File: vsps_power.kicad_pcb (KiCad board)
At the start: 2 copper layers, 84.5 x 85 mm, 11 parts, among them J1 OUT, P1 Conn_WallPlug_Earth, SW1 SW_SPST, T1 Transformer_2P_2S

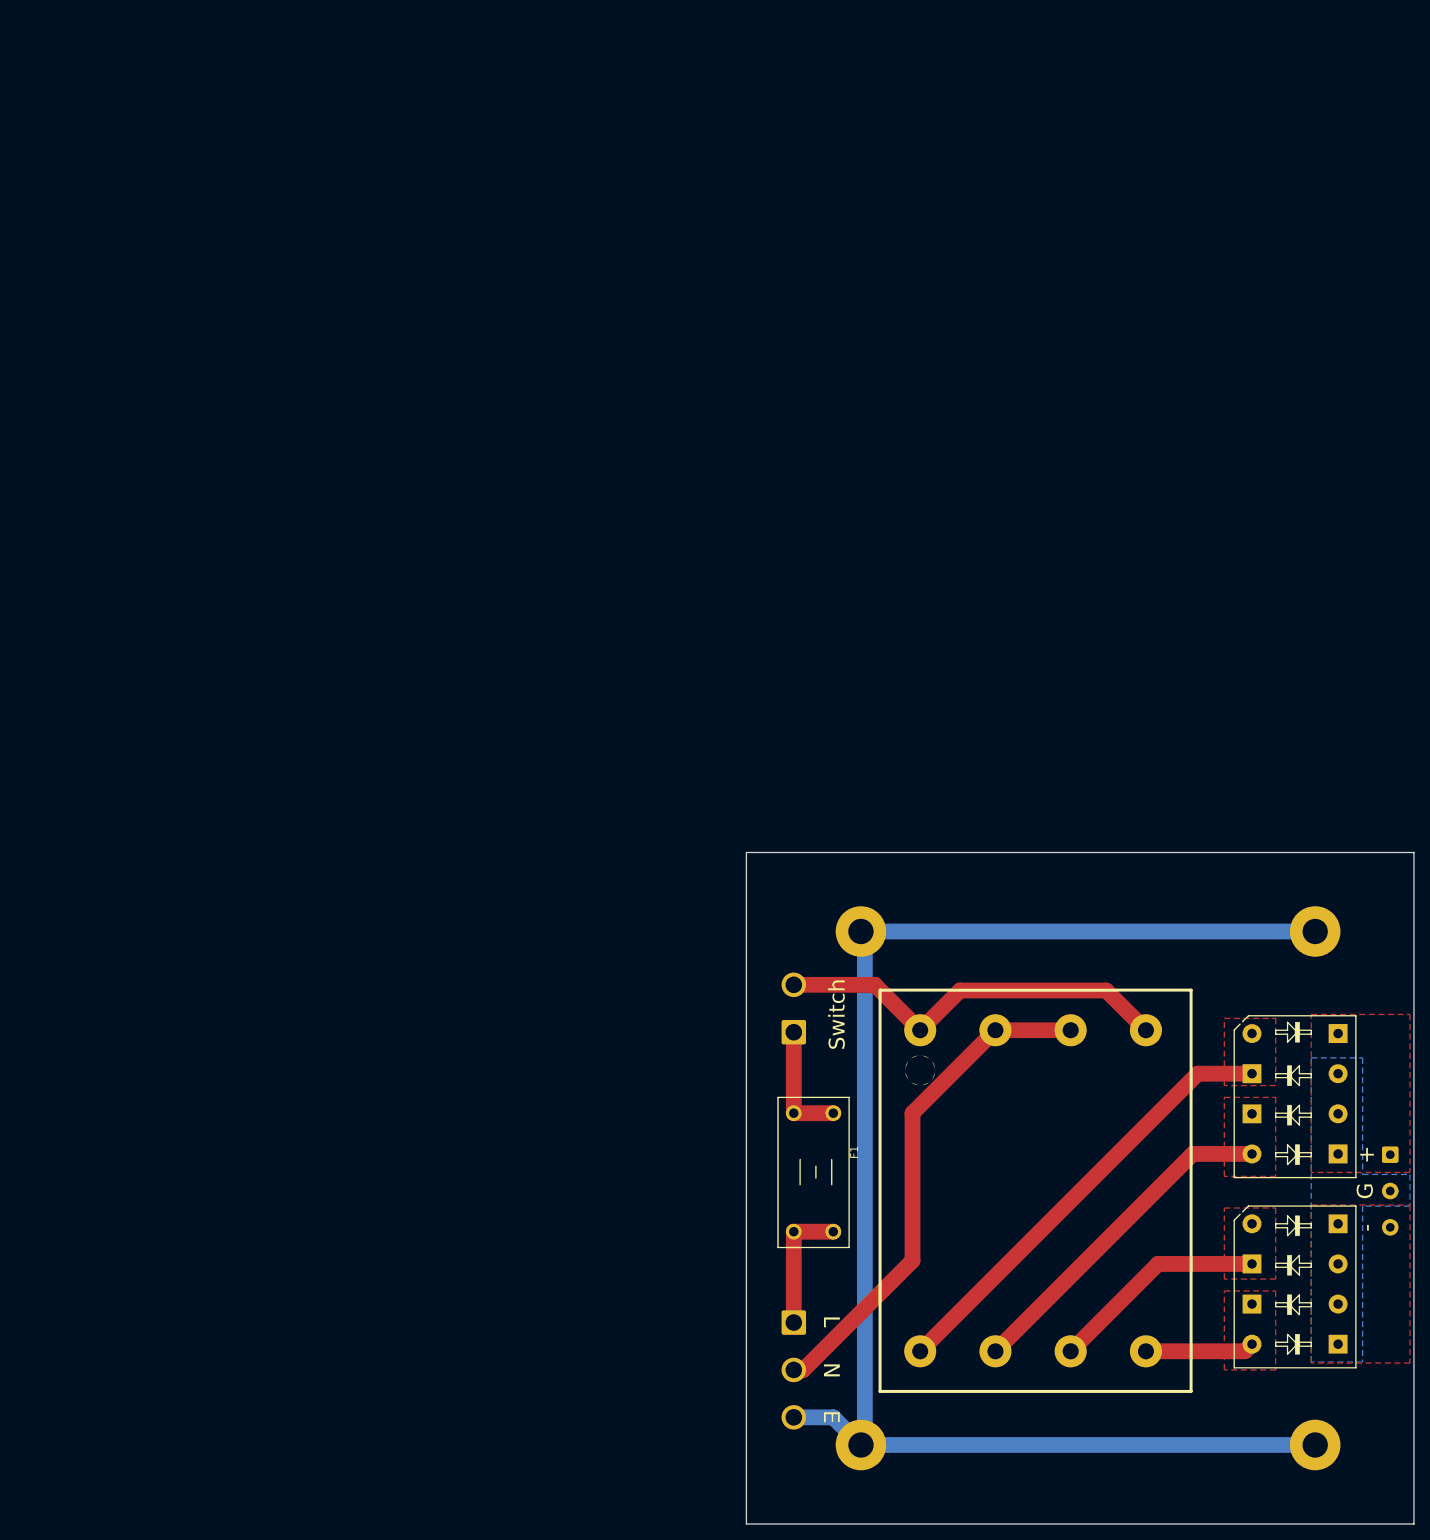
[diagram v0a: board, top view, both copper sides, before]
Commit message: correct transformer footprint
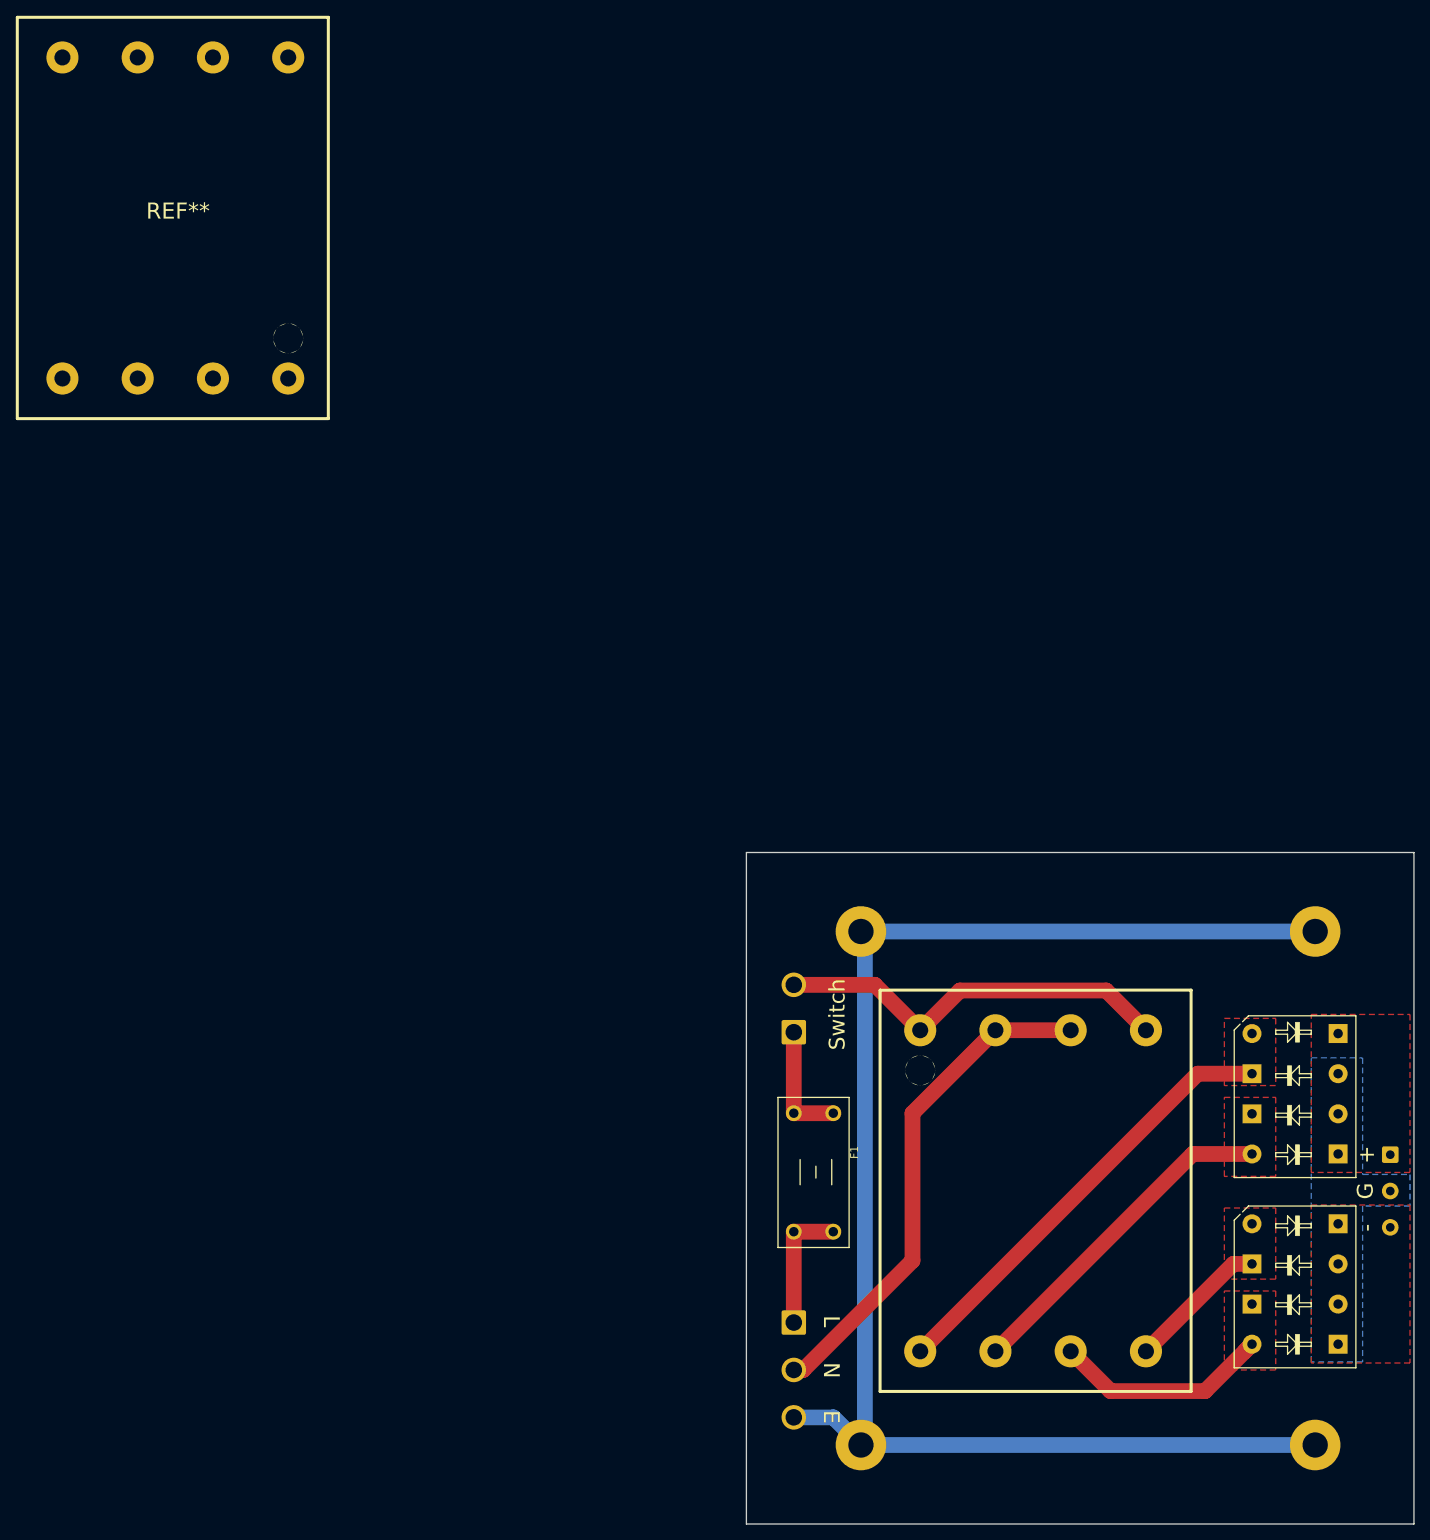
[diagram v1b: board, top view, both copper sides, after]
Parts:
- added REF**: Transformer_Triad_FP24-250, Transformer_THT:Transformer_Triad_FP24-250, F.Cu at (0.00, 0.00)
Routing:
- net Net-(D2-Pad4): track 13.8 -> 28.8 mm
- net Net-(D2-Pad3): track 27.5 -> 18.0 mm
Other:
- net class 115VAC: trace_width 1 -> 2
- net class Default: clearance 0.2 -> 1
- rule trace_clearance: 0.2 -> 1
